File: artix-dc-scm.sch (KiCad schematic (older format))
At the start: 0 parts

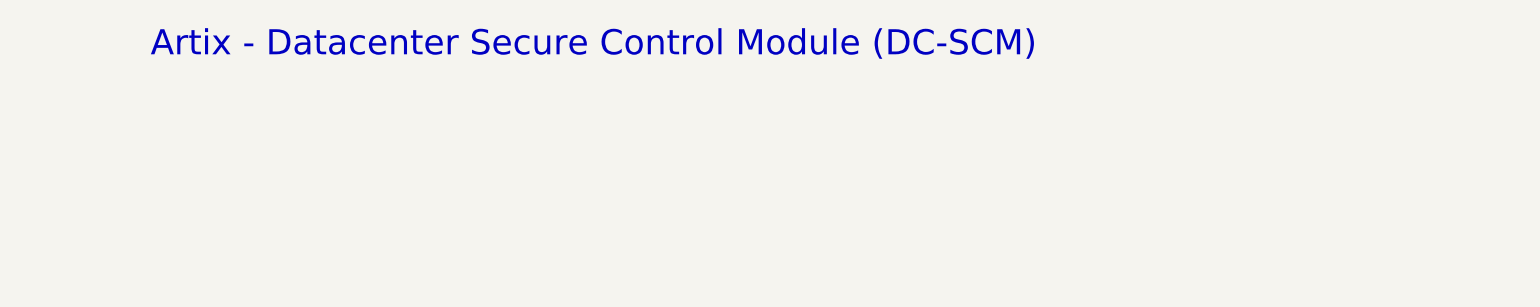
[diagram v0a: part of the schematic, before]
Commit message: Clean M.2 sheet
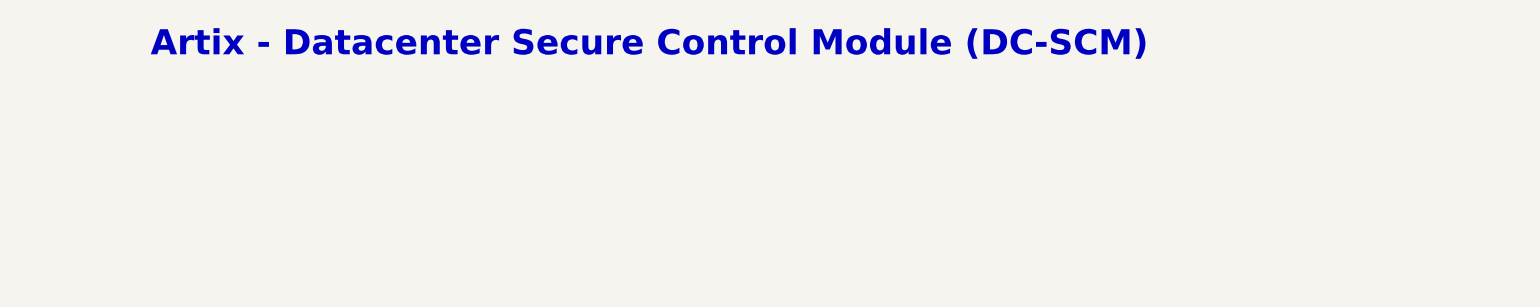
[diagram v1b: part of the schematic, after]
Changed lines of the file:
@@
 Comment4 ""
 $EndDescr
-Text Notes 3400 975  0    118  ~ 0
+Text Notes 3400 975  0    118  ~ 24
 Artix - Datacenter Secure Control Module (DC-SCM)
 $Sheet

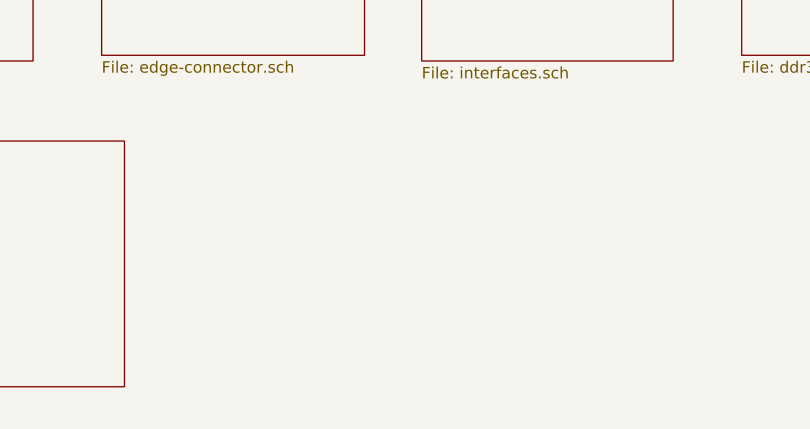
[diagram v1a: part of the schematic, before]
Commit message: Add logotypes and fix DRC errors
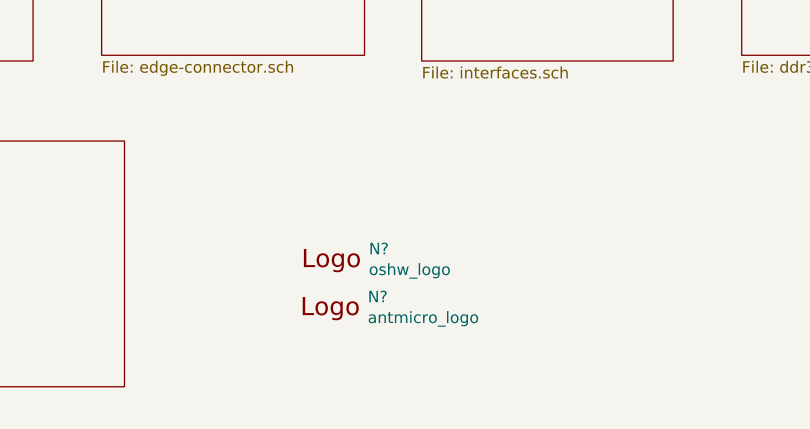
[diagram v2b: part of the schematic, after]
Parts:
- added N?: oshw_logo, antmicro-footprints:oshw-logo, symbol antmicroMechanicalParts:oshw_logo
- added N?: antmicro_logo, antmicro-footprints:antmicro-logo_scaled_20mm, symbol antmicroMechanicalParts:antmicro_logo
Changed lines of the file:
@@
 EndData
 $EndBitmap
+$Comp
+L antmicroMechanicalParts:oshw_logo N?
+U 1 1 6018E5CD
+P 5875 6875
+F 0 "N?" H 6069 6878 50  0000 L CNN
+F 1 "oshw_logo" H 6069 6787 50  0000 L CNN
+F 2 "antmicro-footprints:oshw-logo" H 5895 6635 50  0001 C CNN
+F 3 "" H 5875 6875 50  0001 C CNN
+	1    5875 6875
+	1    0    0    -1
+$EndComp
+$Comp
+L antmicroMechanicalParts:antmicro_logo N?
+U 1 1 6018E8C2
+P 5850 7175
+F 0 "N?" H 6064 7268 50  0000 L CNN
+F 1 "antmicro_logo" H 6064 7177 50  0000 L CNN
+F 2 "antmicro-footprints:antmicro-logo_scaled_20mm" H 5750 7425 50  0001 C CNN
+F 3 "" H 5850 7525 50  0001 C CNN
+	1    5850 7175
+	1    0    0    -1
+$EndComp
 $EndSCHEMATC

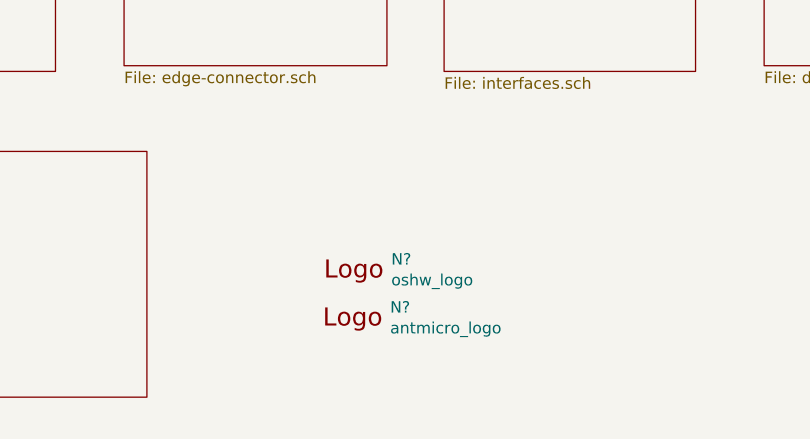
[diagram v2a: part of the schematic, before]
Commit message: Bumped revision to 1.0.1 - replaced ROT connector, added ROT signals and connected to FPGA
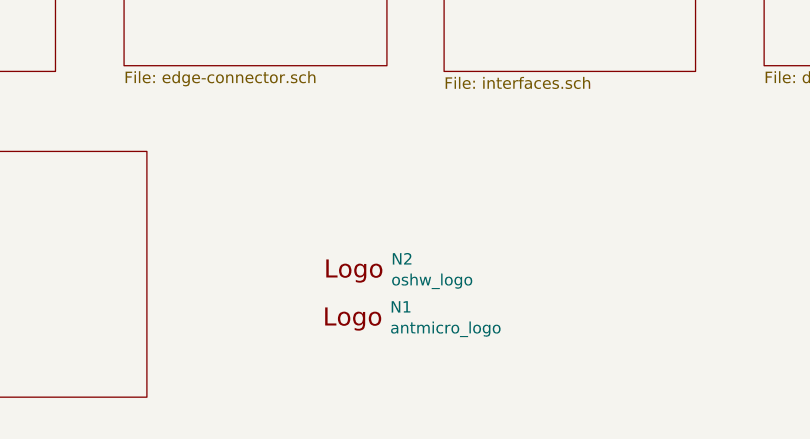
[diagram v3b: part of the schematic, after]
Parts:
- gave numbers to parts that had none: 2
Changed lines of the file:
@@
 Title "Artix - Datacenter Secure Control Module (DC-SCM)"
 Date ""
-Rev "1.0.0"
+Rev "1.0.1"
 Comp ""
 Comment1 ""
@@
 $EndBitmap
 $Comp
-L antmicroMechanicalParts:oshw_logo N?
+L antmicroMechanicalParts:oshw_logo N2
 U 1 1 6018E5CD
 P 5875 6875
-F 0 "N?" H 6069 6878 50  0000 L CNN
+F 0 "N2" H 6069 6878 50  0000 L CNN
 F 1 "oshw_logo" H 6069 6787 50  0000 L CNN
 F 2 "antmicro-footprints:oshw-logo" H 5895 6635 50  0001 C CNN
@@
 $EndComp
 $Comp
-L antmicroMechanicalParts:antmicro_logo N?
+L antmicroMechanicalParts:antmicro_logo N1
 U 1 1 6018E8C2
 P 5850 7175
-F 0 "N?" H 6064 7268 50  0000 L CNN
+F 0 "N1" H 6064 7268 50  0000 L CNN
 F 1 "antmicro_logo" H 6064 7177 50  0000 L CNN
 F 2 "antmicro-footprints:antmicro-logo_scaled_20mm" H 5750 7425 50  0001 C CNN

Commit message: Update edge connector
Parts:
- N1: footprint antmicro-footprints:antmicro-logo_scaled_20mm -> artix-dc-scm-footprints:antmicro-logo_scaled_20mm; symbol antmicroMechanicalParts:antmicro_logo -> artix-dc-scm:antmicro_logo
- N2: footprint antmicro-footprints:oshw-logo -> artix-dc-scm-footprints:oshw-logo; symbol antmicroMechanicalParts:oshw_logo -> artix-dc-scm:oshw_logo
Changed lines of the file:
@@
 $EndBitmap
 $Comp
-L antmicroMechanicalParts:oshw_logo N2
+L artix-dc-scm:oshw_logo N2
 U 1 1 6018E5CD
 P 5875 6875
 F 0 "N2" H 6069 6878 50  0000 L CNN
 F 1 "oshw_logo" H 6069 6787 50  0000 L CNN
-F 2 "antmicro-footprints:oshw-logo" H 5895 6635 50  0001 C CNN
+F 2 "artix-dc-scm-footprints:oshw-logo" H 5895 6635 50  0001 C CNN
 F 3 "" H 5875 6875 50  0001 C CNN
 	1    5875 6875
@@
 $EndComp
 $Comp
-L antmicroMechanicalParts:antmicro_logo N1
+L artix-dc-scm:antmicro_logo N1
 U 1 1 6018E8C2
 P 5850 7175
 F 0 "N1" H 6064 7268 50  0000 L CNN
 F 1 "antmicro_logo" H 6064 7177 50  0000 L CNN
-F 2 "antmicro-footprints:antmicro-logo_scaled_20mm" H 5750 7425 50  0001 C CNN
+F 2 "artix-dc-scm-footprints:antmicro-logo_scaled_20mm" H 5750 7425 50  0001 C CNN
 F 3 "" H 5850 7525 50  0001 C CNN
 	1    5850 7175

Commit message: Fix USB3300 circuit
-remove 1V8 connection
-add capacitance at internal 1v8 regulators
-apply changes to PCB
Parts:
- N1: footprint artix-dc-scm-footprints:antmicro-logo_scaled_20mm -> _autosave-artix-dc-scm-footprints:antmicro-logo_scaled_20mm; symbol artix-dc-scm:antmicro_logo -> _autosave-artix-dc-scm:antmicro_logo
- N2: footprint artix-dc-scm-footprints:oshw-logo -> _autosave-artix-dc-scm-footprints:oshw-logo; symbol artix-dc-scm:oshw_logo -> _autosave-artix-dc-scm:oshw_logo
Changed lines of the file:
@@
 $EndBitmap
 $Comp
-L artix-dc-scm:oshw_logo N2
+L _autosave-artix-dc-scm:oshw_logo N2
 U 1 1 6018E5CD
 P 5875 6875
 F 0 "N2" H 6069 6878 50  0000 L CNN
 F 1 "oshw_logo" H 6069 6787 50  0000 L CNN
-F 2 "artix-dc-scm-footprints:oshw-logo" H 5895 6635 50  0001 C CNN
+F 2 "_autosave-artix-dc-scm-footprints:oshw-logo" H 5895 6635 50  0001 C CNN
 F 3 "" H 5875 6875 50  0001 C CNN
 	1    5875 6875
@@
 $EndComp
 $Comp
-L artix-dc-scm:antmicro_logo N1
+L _autosave-artix-dc-scm:antmicro_logo N1
 U 1 1 6018E8C2
 P 5850 7175
 F 0 "N1" H 6064 7268 50  0000 L CNN
 F 1 "antmicro_logo" H 6064 7177 50  0000 L CNN
-F 2 "artix-dc-scm-footprints:antmicro-logo_scaled_20mm" H 5750 7425 50  0001 C CNN
+F 2 "_autosave-artix-dc-scm-footprints:antmicro-logo_scaled_20mm" H 5750 7425 50  0001 C CNN
 F 3 "" H 5850 7525 50  0001 C CNN
 	1    5850 7175

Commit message: Fixed libs
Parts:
- N1: footprint _autosave-artix-dc-scm-footprints:antmicro-logo_scaled_20mm -> artix-dc-scm-footprints:antmicro-logo_scaled_20mm; symbol _autosave-artix-dc-scm:antmicro_logo -> artix-dc-scm:antmicro_logo
- N2: footprint _autosave-artix-dc-scm-footprints:oshw-logo -> artix-dc-scm-footprints:oshw-logo; symbol _autosave-artix-dc-scm:oshw_logo -> artix-dc-scm:oshw_logo
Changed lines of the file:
@@
 $EndBitmap
 $Comp
-L _autosave-artix-dc-scm:oshw_logo N2
+L artix-dc-scm:oshw_logo N2
 U 1 1 6018E5CD
 P 5875 6875
 F 0 "N2" H 6069 6878 50  0000 L CNN
 F 1 "oshw_logo" H 6069 6787 50  0000 L CNN
-F 2 "_autosave-artix-dc-scm-footprints:oshw-logo" H 5895 6635 50  0001 C CNN
+F 2 "artix-dc-scm-footprints:oshw-logo" H 5895 6635 50  0001 C CNN
 F 3 "" H 5875 6875 50  0001 C CNN
 	1    5875 6875
@@
 $EndComp
 $Comp
-L _autosave-artix-dc-scm:antmicro_logo N1
+L artix-dc-scm:antmicro_logo N1
 U 1 1 6018E8C2
 P 5850 7175
 F 0 "N1" H 6064 7268 50  0000 L CNN
 F 1 "antmicro_logo" H 6064 7177 50  0000 L CNN
-F 2 "_autosave-artix-dc-scm-footprints:antmicro-logo_scaled_20mm" H 5750 7425 50  0001 C CNN
+F 2 "artix-dc-scm-footprints:antmicro-logo_scaled_20mm" H 5750 7425 50  0001 C CNN
 F 3 "" H 5850 7525 50  0001 C CNN
 	1    5850 7175
